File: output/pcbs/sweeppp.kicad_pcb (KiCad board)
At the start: 2 copper layers, 136.5 x 111 mm, 61 parts

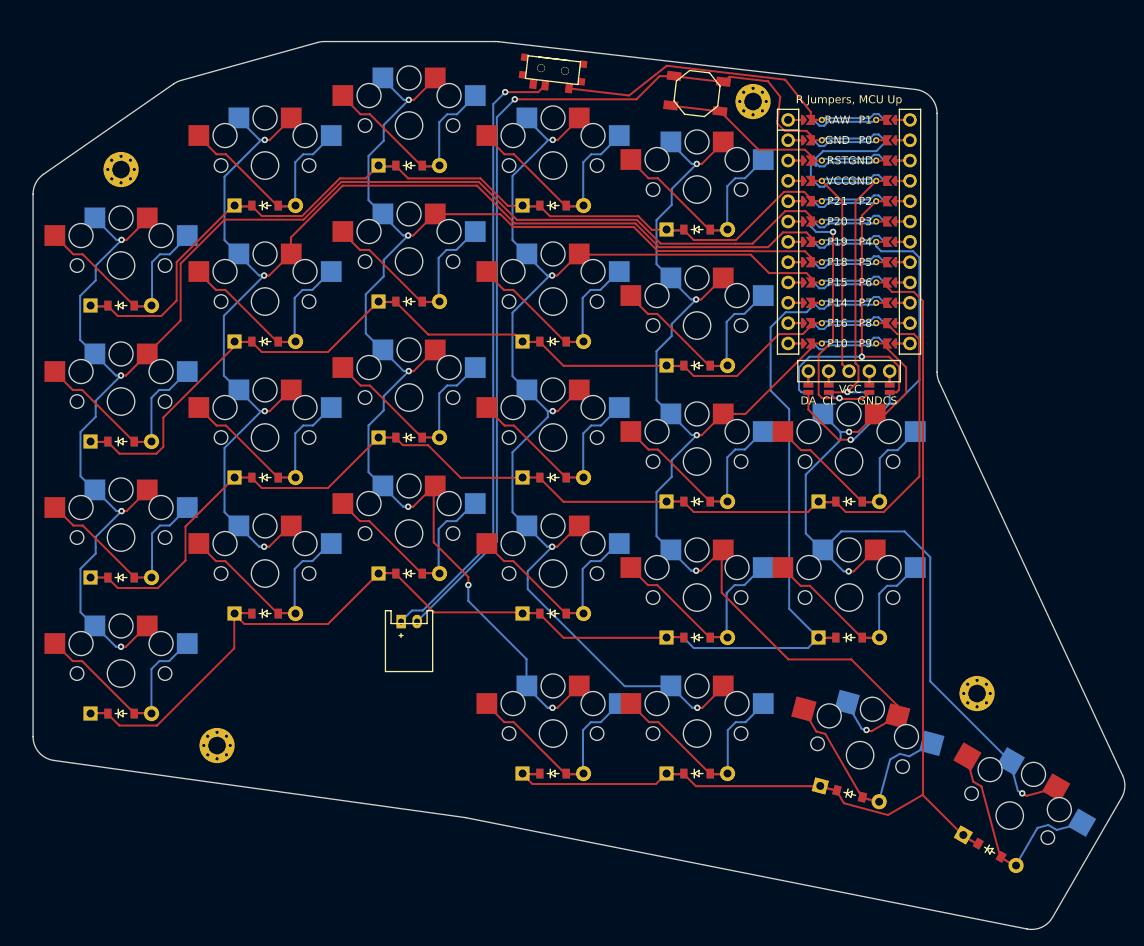
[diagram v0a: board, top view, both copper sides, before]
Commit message: Switch to reversible footprints for jstp, switch, and button
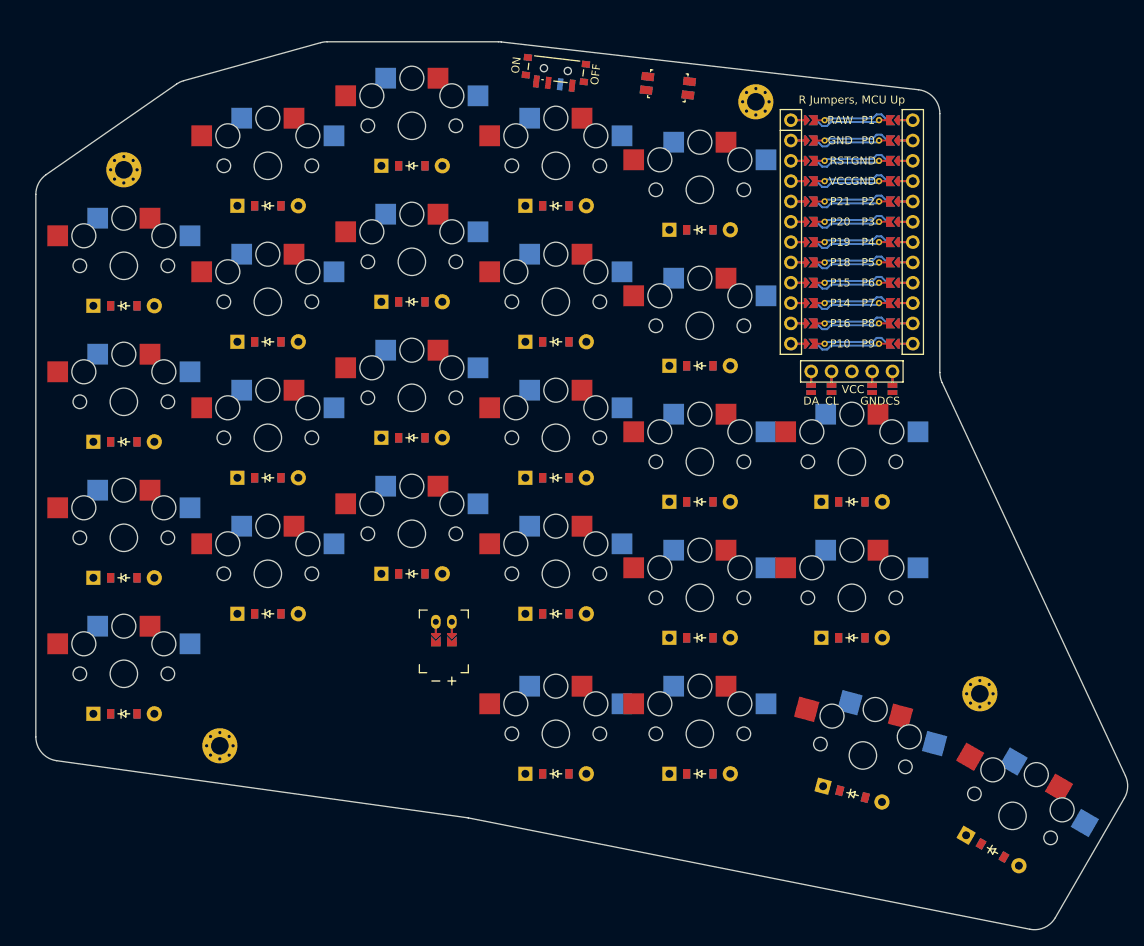
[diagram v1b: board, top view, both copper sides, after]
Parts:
- removed B1: , E73:SW_TACT_ALPS_SKQGABE010
- removed T1: , E73:SPDT_C128955
- added PWR1: , ceoloide:power_switch_smd_side, F.Cu at (154.0, 24.5)
- added RST1: , ceoloide:reset_switch_smd_side, F.Cu at (168.0, 26.5)
- JST1: footprint JST_PH_S2B-PH-K_02x2.00mm_Angled -> ceoloide:battery_connector_jst_ph_2
- moved JST1 4.35 mm to (140.0, 93.5)
- moved S21 0.35 mm to (191.0, 90.5)
- moved D7 0.35 mm to (118.0, 58.5)
- moved D11 0.35 mm to (136.0, 53.5)
- moved D14 0.35 mm to (154.0, 75.5)
- moved D16 0.35 mm to (154.0, 41.5)
- moved D18 0.35 mm to (172.0, 78.5)
- moved D20 0.35 mm to (172.0, 44.5)
- moved D24 0.35 mm to (172.0, 112.5)
- moved DISP1 0.35 mm to (191.0, 45.5)
- moved S10 0.35 mm to (136.0, 65.5)
- moved S13 0.35 mm to (154.0, 87.5)
- moved S15 0.35 mm to (154.0, 53.5)
- moved S12 0.35 mm to (136.0, 31.5)
- moved D4 0.35 mm to (100.0, 54.0)
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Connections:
- JST1 pad 1: BAT -> BAT_P
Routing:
- net (no net): track 0.00 -> 337.7 mm
- net P20: track 198.9 -> 0.00 mm, vias 4 -> 0
- net GND: track 191.8 -> 3.50 mm, vias 2 -> 0
- net P18: track 187.9 -> 0.00 mm, vias 6 -> 0
- net P7: track 182.5 -> 0.00 mm
- net P19: track 173.4 -> 0.00 mm, vias 4 -> 0
- net P8: track 167.1 -> 0.00 mm
- net P15: track 166.9 -> 0.00 mm, vias 5 -> 0
- net P10: track 155.3 -> 0.00 mm, vias 5 -> 0
- net P6: track 151.0 -> 0.00 mm
- net P21: track 129.9 -> 0.00 mm
- net P16: track 129.6 -> 0.00 mm
- net P9: track 112.0 -> 0.00 mm, vias 3 -> 0
- net BAT: track 77.7 -> 0.00 mm, vias 1 -> 0
- net P4: track 53.8 -> 3.50 mm, vias 1 -> 0
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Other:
- net class Default added: clearance 0.2, trace_width 0.25, via_dia 0.8, via_drill 0.4

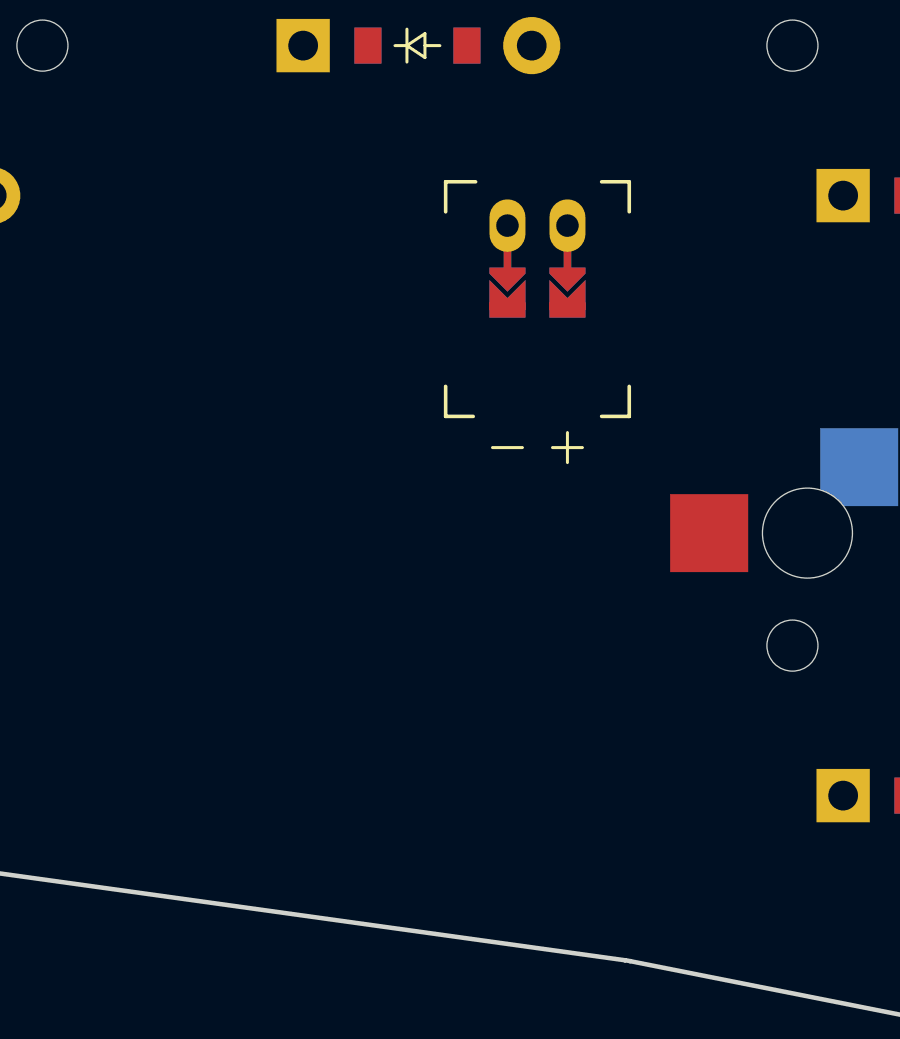
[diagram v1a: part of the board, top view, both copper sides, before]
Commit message: moved jst
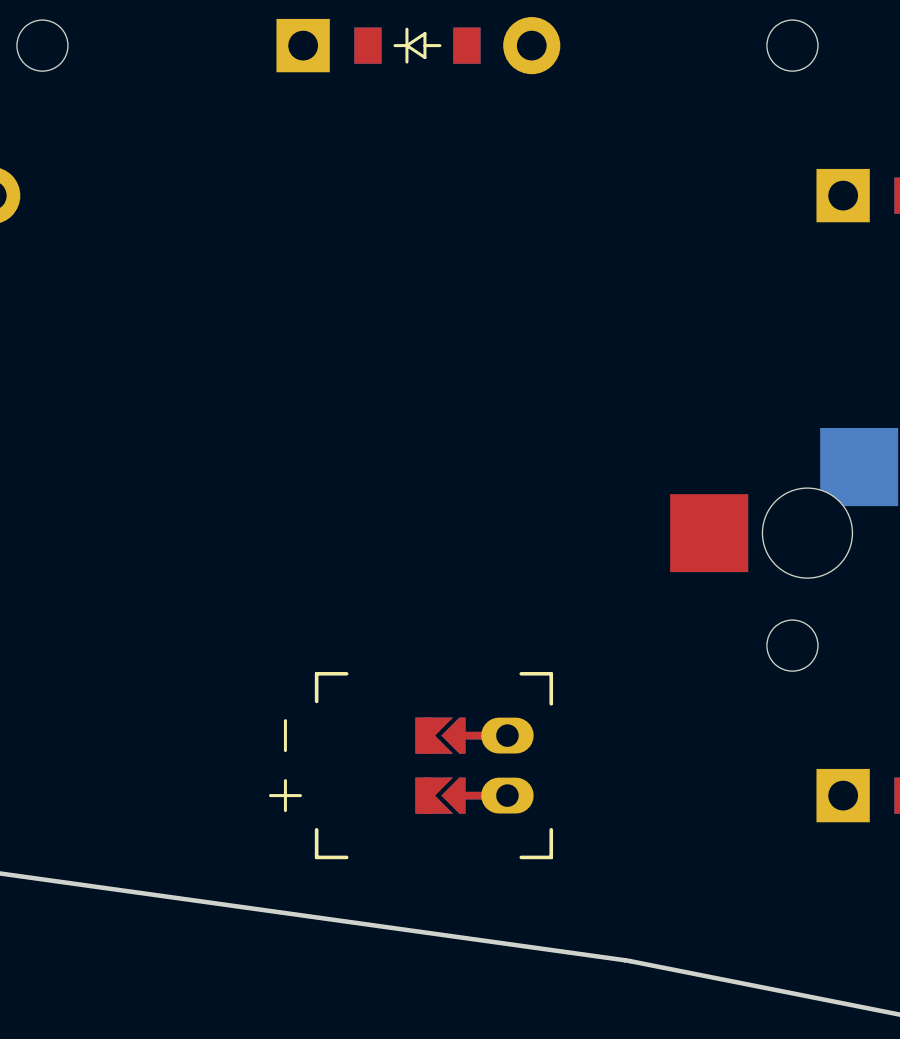
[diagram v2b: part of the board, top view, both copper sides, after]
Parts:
- moved JST1 18.0 mm to (139.0, 111.5), turned to -90 degrees
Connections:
- PWR1 pad 1: RAW -> BAT_P
- PWR1 pad 2: BAT -> RAW
- PWR1 pad 3: RAW -> BAT_P
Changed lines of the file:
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@@
 (net 78 "DISP1_4")
 (net 79 "DISP1_5")
-(net 80 "BAT")
-(net 81 "BAT_P")
-(net 82 "JST1_1")
-(net 83 "JST1_2")
+(net 80 "BAT_P")
+(net 81 "JST1_1")
+(net 82 "JST1_2")
   (net_class Default "This is the default net class."
     (clearance 0.2)
@@
 (add_net "DISP1_4")
 (add_net "DISP1_5")
-(add_net "BAT")
 (add_net "BAT_P")
 (add_net "JST1_1")
@@
     (pad "" smd rect (at 1.125 3.65 173.3) (size 1 0.8) (layers "F.Cu" "F.Paste" "F.Mask"))
     (pad "1" smd rect (at -1.735 2.25 173.3) (size 0.7 1.5) (layers "F.Cu" "F.Paste" "F.Mask") )
-    (pad "2" smd rect (at -1.735 -0.75 173.3) (size 0.7 1.5) (layers "F.Cu" "F.Paste" "F.Mask") (net 80 "BAT"))
-    (pad "3" smd rect (at -1.735 -2.25 173.3) (size 0.7 1.5) (layers "F.Cu" "F.Paste" "F.Mask") (net 38 "RAW"))
+    (pad "2" smd rect (at -1.735 -0.75 173.3) (size 0.7 1.5) (layers "F.Cu" "F.Paste" "F.Mask") (net 38 "RAW"))
+    (pad "3" smd rect (at -1.735 -2.25 173.3) (size 0.7 1.5) (layers "F.Cu" "F.Paste" "F.Mask") (net 80 "BAT_P"))
     (fp_text user "ON" (at 0 -5 83.3) (layer "F.SilkS")
       (effects (font (size 1 1) (thickness 0.15)))
@@
     (pad "" smd rect (at -1.085 3.65 353.3) (size 1 0.8) (layers "B.Cu" "B.Paste" "B.Mask"))
     (pad "" smd rect (at 1.125 3.65 353.3) (size 1 0.8) (layers "B.Cu" "B.Paste" "B.Mask"))
-    (pad "1" smd rect (at -1.735 -2.25 353.3) (size 0.7 1.5) (layers "B.Cu" "B.Paste" "B.Mask") (net 38 "RAW"))
-    (pad "2" smd rect (at -1.735 0.75 353.3) (size 0.7 1.5) (layers "B.Cu" "B.Paste" "B.Mask") (net 80 "BAT"))
+    (pad "1" smd rect (at -1.735 -2.25 353.3) (size 0.7 1.5) (layers "B.Cu" "B.Paste" "B.Mask") (net 80 "BAT_P"))
+    (pad "2" smd rect (at -1.735 0.75 353.3) (size 0.7 1.5) (layers "B.Cu" "B.Paste" "B.Mask") (net 38 "RAW"))
     (pad "3" smd rect (at -1.735 2.25 353.3) (size 0.7 1.5) (layers "B.Cu" "B.Paste" "B.Mask") )
     (fp_text user "PWR1" (at -3.5 0 173.3) (layer "B.SilkS") hide
@@
     (footprint "ceoloide:battery_connector_jst_ph_2"
         (layer "F.Cu")
-        (at 140 93.5 0)
+        (at 139 111.5 -90)
         (property "Reference" "JST1"
-            (at 0 4.8 0)
+            (at 0 4.8 -90)
             (layer "F.SilkS")
             hide
@@
         (fp_line (start 2.14 6.36) (end 3.06 6.36) (stroke (width 0.12) (type solid)) (layer "B.SilkS"))
         (fp_line (start 3.06 6.36) (end 3.06 5.36) (stroke (width 0.12) (type solid)) (layer "B.SilkS"))
-        (pad "11" thru_hole oval (at -1 0 0) (size 1.2 1.75) (drill 0.75) (layers "*.Cu" "*.Mask") (net 82 "JST1_1"))
-        (pad "12" thru_hole oval (at 1 0 0) (size 1.2 1.75) (drill 0.75) (layers "*.Cu" "*.Mask") (net 83 "JST1_2"))
-        (pad "21" smd custom (at -1 1.8 180) (size 0.1 0.1) (layers "F.Cu" "F.Mask" "F.Paste")
+        (pad "11" thru_hole oval (at -1 0 -90) (size 1.2 1.75) (drill 0.75) (layers "*.Cu" "*.Mask") (net 81 "JST1_1"))
+        (pad "12" thru_hole oval (at 1 0 -90) (size 1.2 1.75) (drill 0.75) (layers "*.Cu" "*.Mask") (net 82 "JST1_2"))
+        (pad "21" smd custom (at -1 1.8 90) (size 0.1 0.1) (layers "F.Cu" "F.Mask" "F.Paste")
             (clearance 0.1) (zone_connect 0)
             (options (clearance outline) (anchor rect))
@@
                 )
             )
-            (net 82 "JST1_1")
+            (net 81 "JST1_1")
         )
-        (pad "31" smd custom (at -1 1.8 180) (size 0.1 0.1) (layers "B.Cu" "B.Mask" "B.Paste")
+        (pad "31" smd custom (at -1 1.8 90) (size 0.1 0.1) (layers "B.Cu" "B.Mask" "B.Paste")
             (clearance 0.1) (zone_connect 0)
             (options (clearance outline) (anchor rect))
@@
                 )
             )
-            (net 82 "JST1_1")
+            (net 81 "JST1_1")
         )
-        (pad "22" smd custom (at 1 1.8 180) (size 0.1 0.1) (layers "F.Cu" "F.Mask" "F.Paste")
+        (pad "22" smd custom (at 1 1.8 90) (size 0.1 0.1) (layers "F.Cu" "F.Mask" "F.Paste")
             (clearance 0.1) (zone_connect 0)
             (options (clearance outline) (anchor rect))
@@
                 )
             )
-            (net 83 "JST1_2")
+            (net 82 "JST1_2")
         )
-        (pad "32" smd custom (at 1 1.8 180) (size 0.1 0.1) (layers "B.Cu" "B.Mask" "B.Paste")
+        (pad "32" smd custom (at 1 1.8 90) (size 0.1 0.1) (layers "B.Cu" "B.Mask" "B.Paste")
             (clearance 0.1) (zone_connect 0)
             (options (clearance outline) (anchor rect))
@@
                 )
             )
-            (net 83 "JST1_2")
+            (net 82 "JST1_2")
         )
-        (pad "1" smd custom (at -1 2.816 180) (size 1.2 0.5) (layers "F.Cu" "F.Mask" "F.Paste") (net 81 "BAT_P")
+        (pad "1" smd custom (at -1 2.816 90) (size 1.2 0.5) (layers "F.Cu" "F.Mask" "F.Paste") (net 80 "BAT_P")
             (clearance 0.1) (zone_connect 0)
             (options (clearance outline) (anchor rect))
@@
             )
         )
-        (pad "1" smd custom (at 1 2.816 180) (size 1.2 0.5) (layers "B.Cu" "B.Mask" "B.Paste") (net 81 "BAT_P")
+        (pad "1" smd custom (at 1 2.816 90) (size 1.2 0.5) (layers "B.Cu" "B.Mask" "B.Paste") (net 80 "BAT_P")
             (clearance 0.1) (zone_connect 0)
             (options (clearance outline) (anchor rect))
@@
             )
         )
-        (pad "2" smd custom (at -1 2.816 180) (size 1.2 0.5) (layers "B.Cu" "B.Mask" "B.Paste") (net 39 "GND")
+        (pad "2" smd custom (at -1 2.816 90) (size 1.2 0.5) (layers "B.Cu" "B.Mask" "B.Paste") (net 39 "GND")
             (clearance 0.1) (zone_connect 0)
             (options (clearance outline) (anchor rect))
@@
             )
         )
-        (pad "2" smd custom (at 1 2.816 180) (size 1.2 0.5) (layers "F.Cu" "F.Mask" "F.Paste") (net 39 "GND")
+        (pad "2" smd custom (at 1 2.816 90) (size 1.2 0.5) (layers "F.Cu" "F.Mask" "F.Paste") (net 39 "GND")
             (clearance 0.1) (zone_connect 0)
             (options (clearance outline) (anchor rect))
@@
         )
     )
-    (segment (start 139 95.3) (end 139 93.5) (width 0.25) (layer "F.Cu") (net 82))
-    (segment (start 139 95.3) (end 139 93.5) (width 0.25) (layer "B.Cu") (net 82))
-    (segment (start 141 95.3) (end 141 93.5) (width 0.25) (layer "F.Cu") (net 83))
-    (segment (start 141 95.3) (end 141 93.5) (width 0.25) (layer "B.Cu") (net 83))
+    (segment (start 137.2 110.5) (end 139 110.5) (width 0.25) (layer "F.Cu") (net 81))
+    (segment (start 137.2 110.5) (end 139 110.5) (width 0.25) (layer "B.Cu") (net 81))
+    (segment (start 137.2 112.5) (end 139 112.5) (width 0.25) (layer "F.Cu") (net 82))
+    (segment (start 137.2 112.5) (end 139 112.5) (width 0.25) (layer "B.Cu") (net 82))
     (module "MountingHole_2.2mm_M2_Pad_Via" (version 20210722) (generator pcbnew) (layer "F.Cu")
       (at 100 37 0)

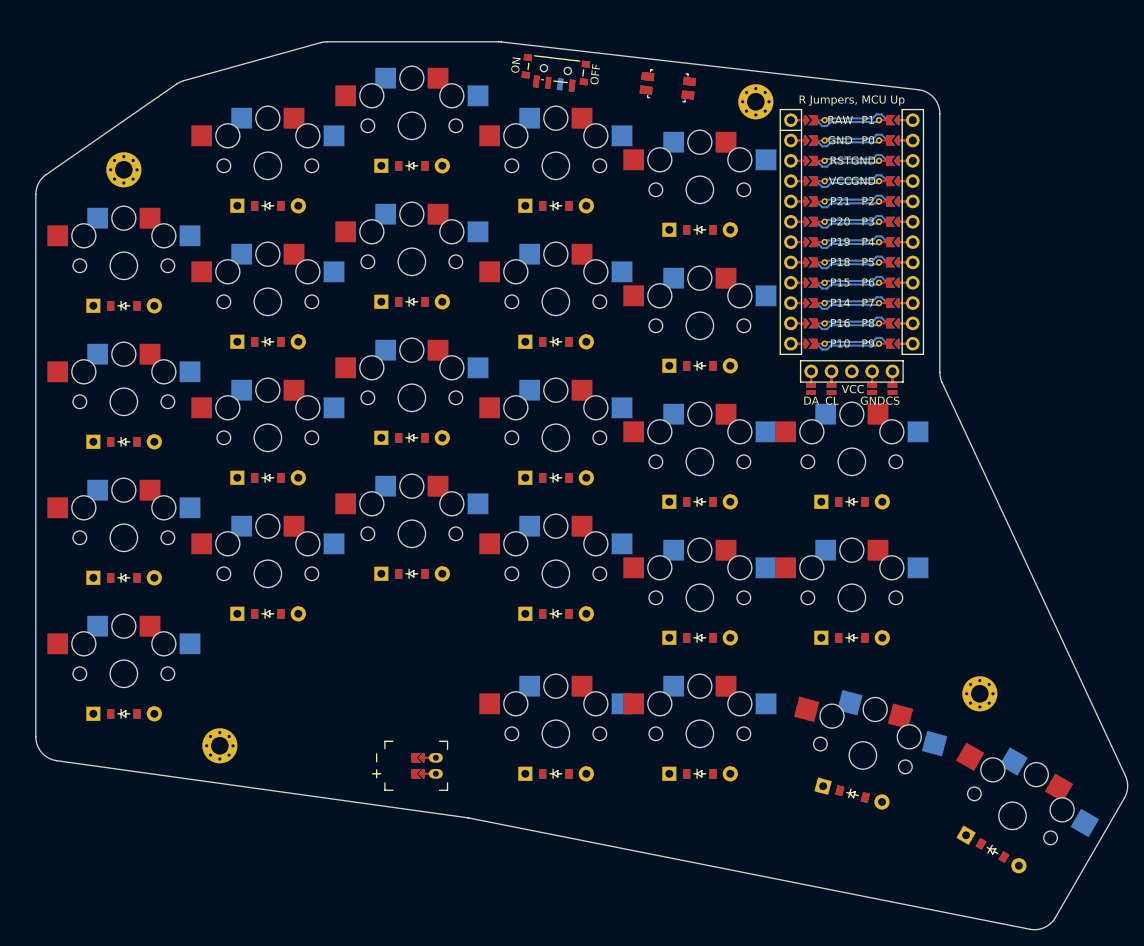
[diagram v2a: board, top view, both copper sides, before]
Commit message: Added traces
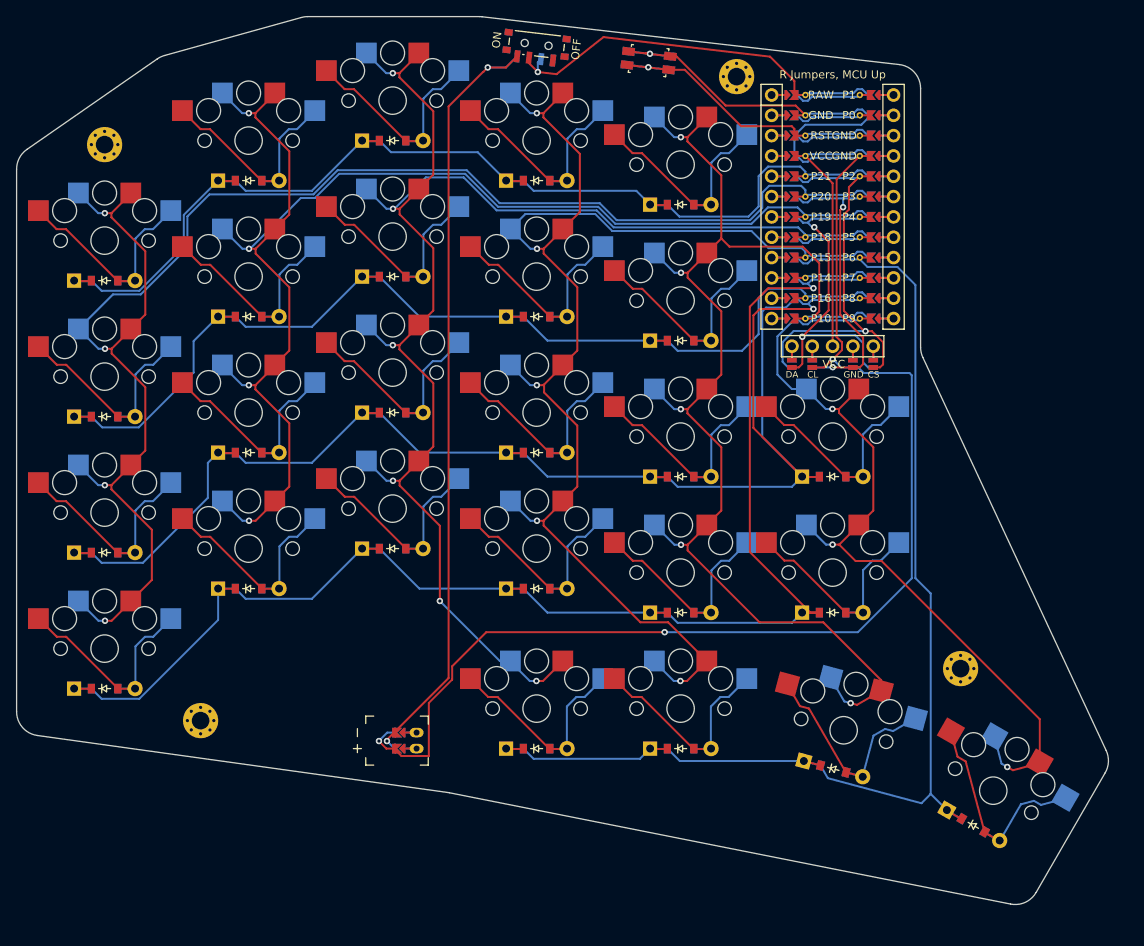
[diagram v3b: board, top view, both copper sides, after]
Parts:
- moved _1 3.96 mm to (97.6, 33.9)
- moved MCU1 3.96 mm to (188.6, 40.4)
- moved D9 3.96 mm to (133.6, 84.4)
- moved S19 3.96 mm to (169.6, 53.4)
- moved S25 3.96 mm to (190.0, 107.1)
- moved DISP1 3.96 mm to (188.6, 42.4)
- moved S10 3.96 mm to (133.6, 62.4)
- moved S22 3.96 mm to (188.6, 70.4)
- moved S5 3.96 mm to (115.6, 84.4)
- moved S7 3.96 mm to (115.6, 50.4)
- moved D14 3.96 mm to (151.6, 72.4)
- moved D22 3.96 mm to (188.6, 75.4)
- moved S21 3.96 mm to (188.6, 87.4)
- moved D5 3.96 mm to (115.6, 89.4)
- moved D19 3.96 mm to (169.6, 58.4)
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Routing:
- net (no net): track 337.7 -> 0.00 mm
- net GND: track 3.50 -> 223.4 mm, vias 0 -> 4
- net P20: track 0.00 -> 203.8 mm, vias 0 -> 4
- net P8: track 0.00 -> 191.2 mm, vias 0 -> 1
- net P18: track 0.00 -> 189.2 mm, vias 0 -> 6
- net P7: track 0.00 -> 184.3 mm, vias 0 -> 1
- net P19: track 0.00 -> 172.6 mm, vias 0 -> 4
- net P15: track 0.00 -> 172.4 mm, vias 0 -> 5
- net P10: track 0.00 -> 158.4 mm, vias 0 -> 5
- net P6: track 0.00 -> 153.7 mm
- net P16: track 0.00 -> 134.3 mm
- net P21: track 0.00 -> 133.3 mm
- net P9: track 0.00 -> 104.4 mm, vias 0 -> 3
- net BAT_P: track 0.00 -> 99.2 mm, vias 0 -> 2
- net RAW: track 0.00 -> 50.7 mm, vias 0 -> 1
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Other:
- net class Default removed
